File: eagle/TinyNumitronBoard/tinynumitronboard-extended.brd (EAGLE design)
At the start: 100 x 50 mm, 47 parts

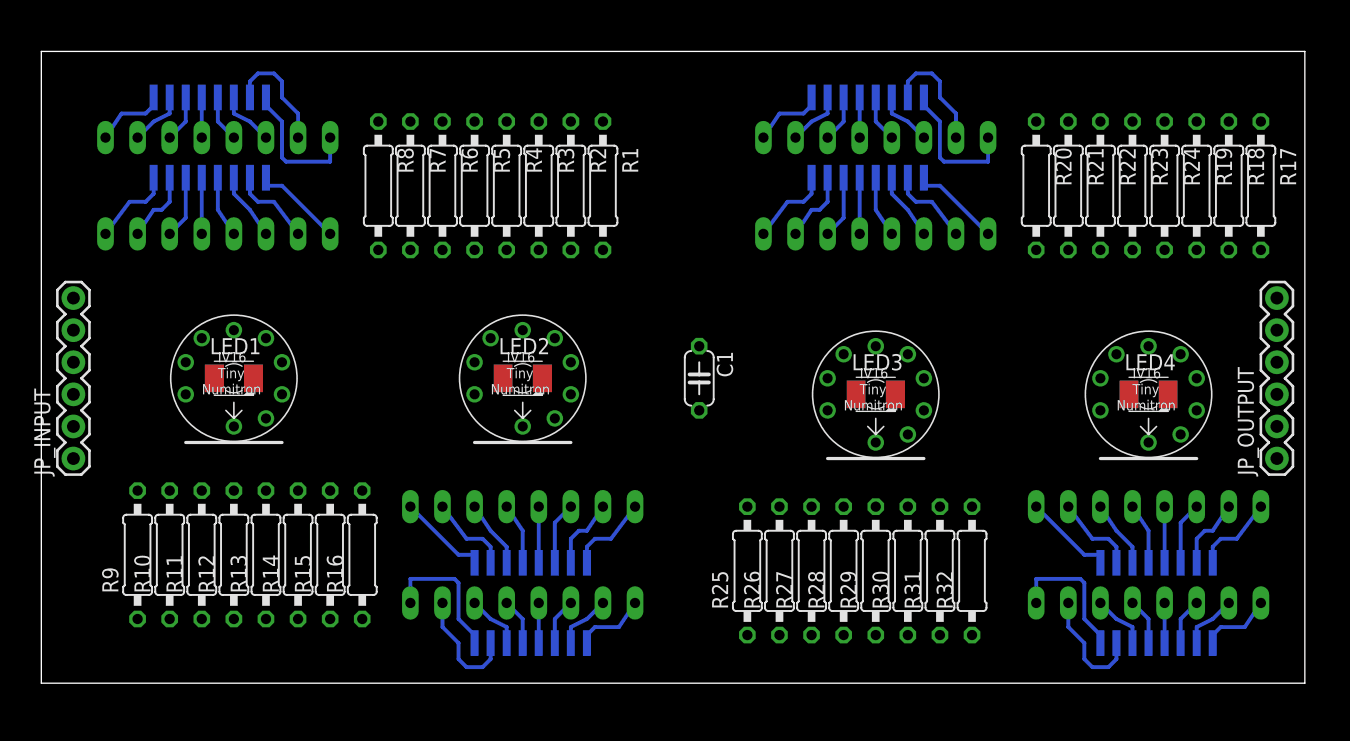
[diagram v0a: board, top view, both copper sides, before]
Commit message: added mounting holes and improved placement.
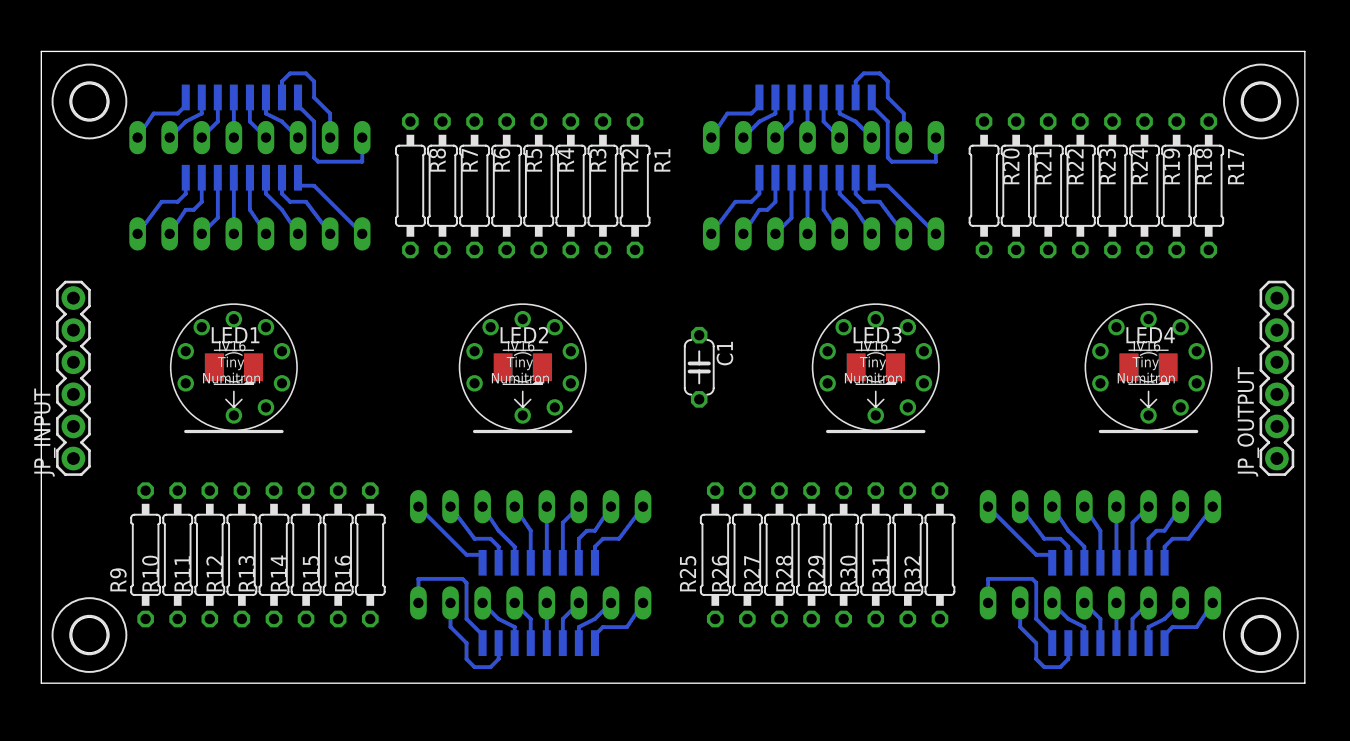
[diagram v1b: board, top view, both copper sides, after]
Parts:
- added H1, H2, H3, H4: MOUNT-HOLE2.8, holes:2,8
- moved R24 4.13 mm to (84.8, 39.4)
- moved U$6 4.13 mm to (61.9, 40.6)
- moved R17 4.13 mm to (92.4, 39.4)
- moved R18 4.13 mm to (89.9, 39.4)
- moved R19 4.13 mm to (87.3, 39.4)
- moved R20 4.13 mm to (74.6, 39.4)
- moved R21 4.13 mm to (77.2, 39.4)
- moved R22 4.13 mm to (79.7, 39.4)
- moved R23 4.13 mm to (82.2, 39.4)
- moved U$8 3.81 mm to (83.8, 8.89)
- moved R29 2.84 mm to (63.5, 10.2)
- moved R31 2.84 mm to (68.6, 10.2)
- moved R25 2.84 mm to (53.3, 10.2)
- moved R26 2.84 mm to (55.9, 10.2)
- moved R27 2.84 mm to (58.4, 10.2)
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
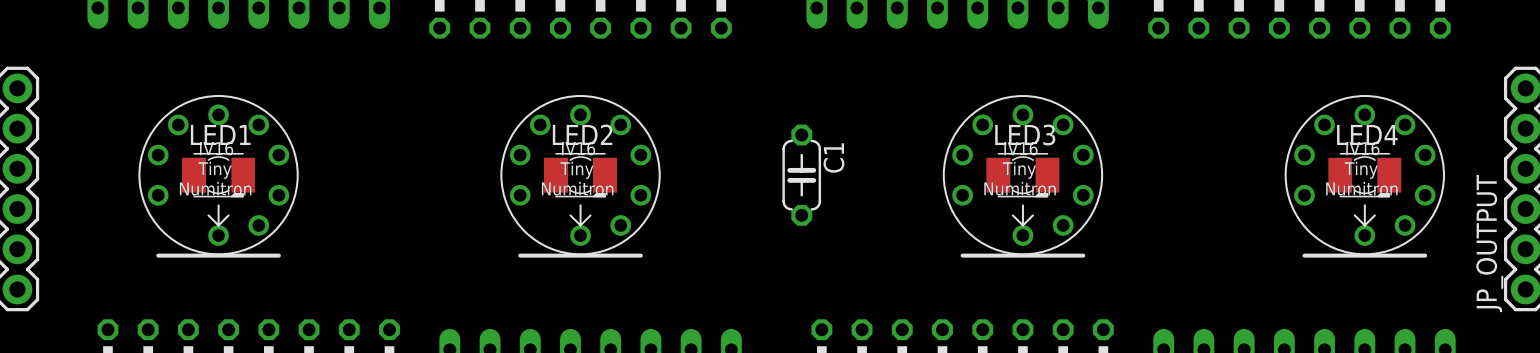
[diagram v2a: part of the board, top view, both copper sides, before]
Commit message: fixed the lots of missing wires ! all connections should be ok now.
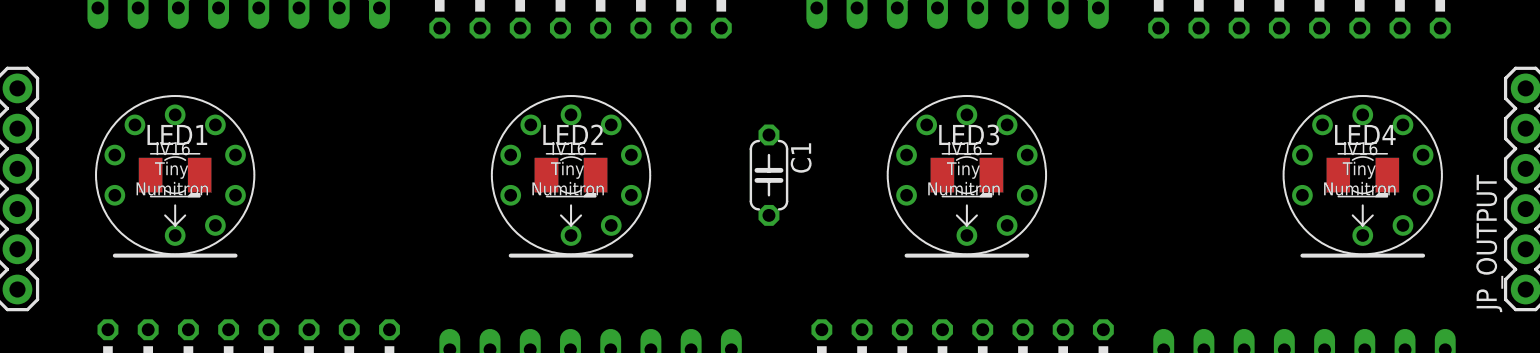
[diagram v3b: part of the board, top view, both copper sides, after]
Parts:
- moved U$2 49.4 mm to (87.5, 25.0)
- moved U$5 28.5 mm to (37.5, 25.0)
- moved U$7 25.1 mm to (62.5, 25.0)
- moved LED3 3.54 mm to (62.5, 25.0)
- moved LED1 2.74 mm to (12.5, 25.0)
- moved U$1 2.74 mm to (12.5, 25.0)
- moved C1 2.07 mm to (50.0, 25.0)
- moved LED2 0.60 mm to (37.5, 25.0)
- moved LED4 0.13 mm to (87.5, 25.0)
- renumbered U$3 to UC1, U$4 to UC4, U$6 to UC2, U$8 to UC3
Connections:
- removed net N$15: JP_INPUT.5, JP_INPUT.6
- removed net N$18: C1.1, JP_INPUT.4, JP_OUTPUT.4, UC4.12, UC4.S12
- removed net N$19: JP_INPUT.3, JP_OUTPUT.3, UC4.11, UC4.S11
- new net N$23: UC1.9, UC1.S9, UC2.14, UC2.S14
- new net N$58: UC2.9, UC2.S9, UC3.14, UC3.S14
- new net RCK: C1.1, JP_INPUT.4, JP_OUTPUT.4, UC1.12, UC1.S12, UC2.12, UC2.S12, UC3.12, UC3.S12, UC4.12, UC4.S12
- new net SCK: JP_INPUT.3, JP_OUTPUT.3, UC1.11, UC1.S11, UC2.11, UC2.S11, UC3.11, UC3.S11, UC4.11, UC4.S11
- new net SER: JP_INPUT.5, JP_INPUT.6, UC1.14, UC1.S14
- net GND: now also UC1.13, UC1.S13, UC2.13, UC2.S13, UC3.13, UC3.S13
- net N$37: now also LED4.A; no longer LED2.A
- net N$54: now also LED2.A; no longer LED3.A
- net N$77: now also LED3.A; no longer LED4.A
- net N$78: now also UC3.9, UC3.S9
- net VCC: now also UC1.10, UC1.S10, UC2.10, UC2.S10, UC3.10, UC3.S10

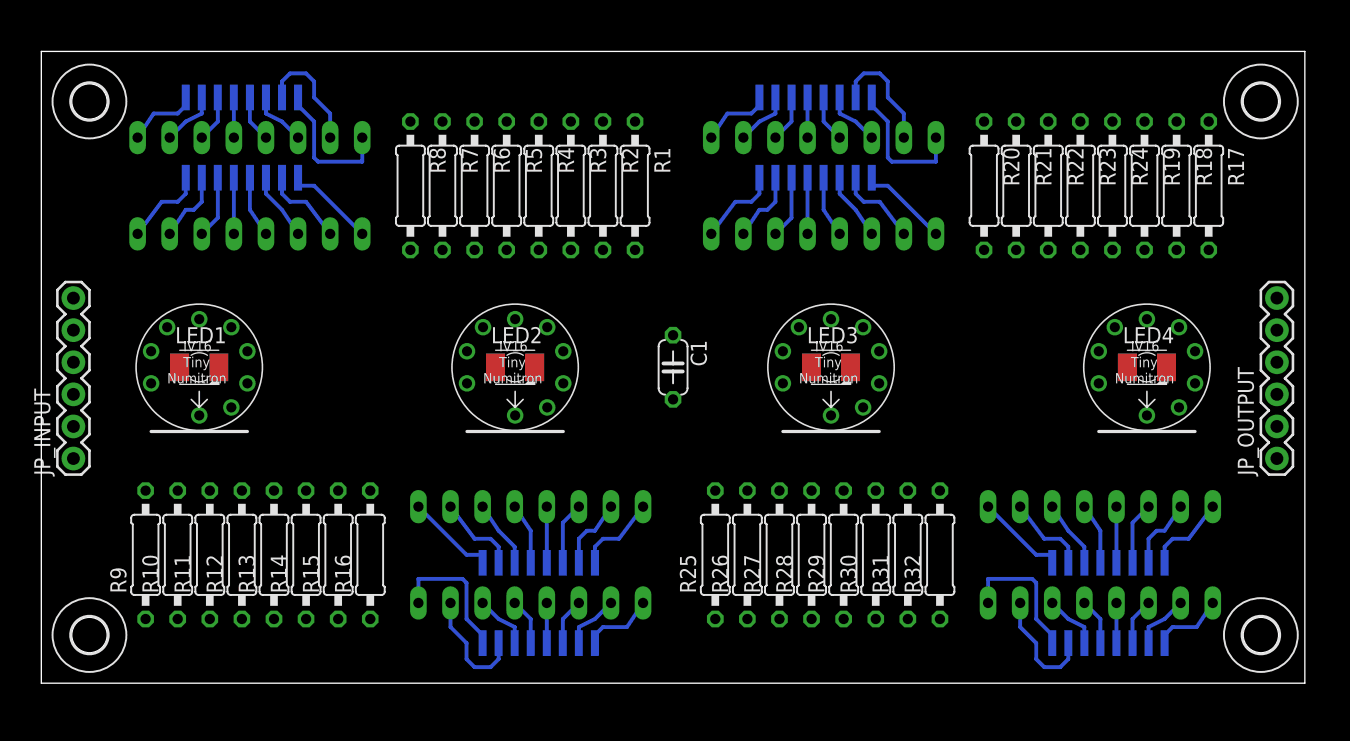
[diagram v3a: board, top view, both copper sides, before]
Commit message: Improved component placement.
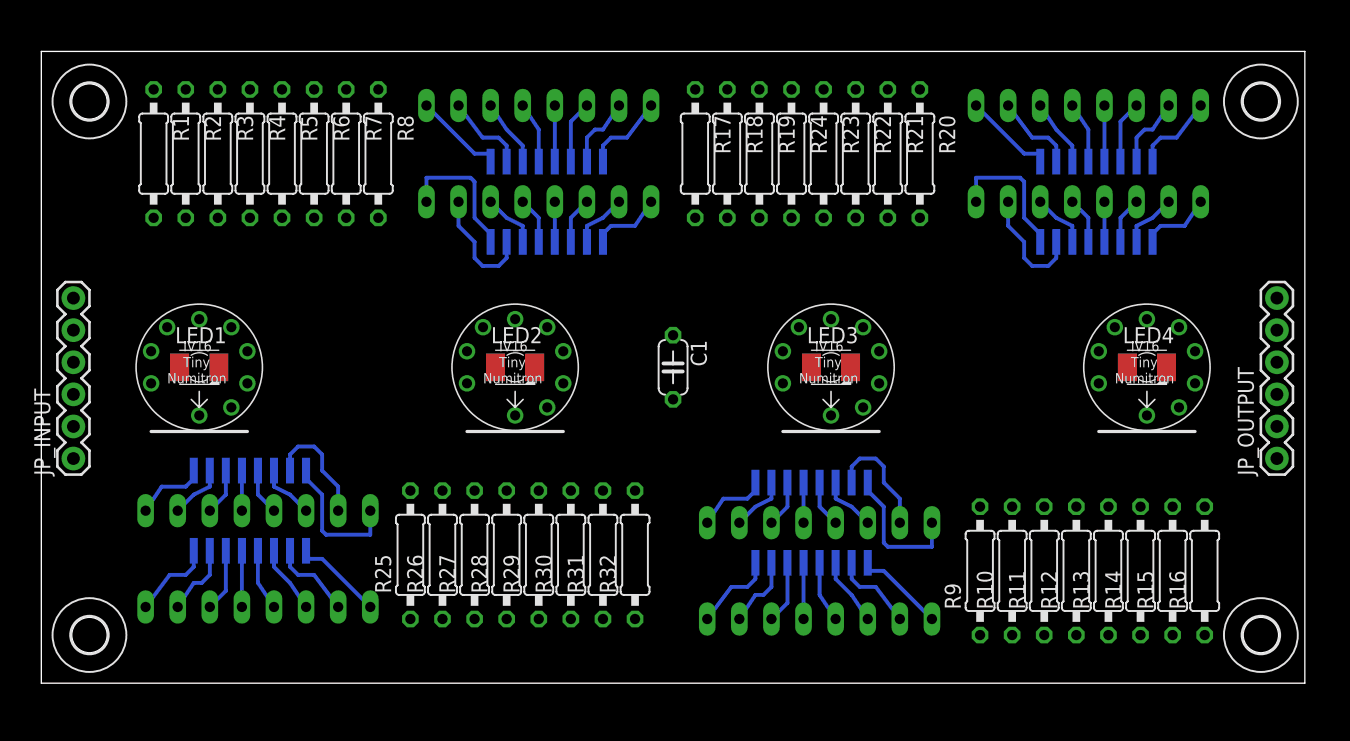
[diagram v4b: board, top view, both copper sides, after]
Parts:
- moved UC3 66.7 mm to (17.1, 11.1), turned to 180 degrees
- moved R12 66.1 mm to (81.9, 8.89)
- moved R14 66.1 mm to (87.0, 8.89)
- moved R16 66.1 mm to (92.1, 8.89)
- moved R9 66.1 mm to (74.3, 8.89)
- moved R10 66.1 mm to (76.8, 8.89)
- moved R11 66.1 mm to (79.4, 8.89)
- moved R13 66.1 mm to (84.5, 8.89)
- moved R15 66.1 mm to (89.5, 8.89)
- moved R17 40.7 mm to (51.8, 41.9)
- moved R1 38.2 mm to (8.89, 41.9)
- moved R18 35.7 mm to (54.3, 41.9)
- moved R2 33.1 mm to (11.4, 41.9)
- moved R19 30.6 mm to (56.8, 41.9)
- moved R3 28.1 mm to (14.0, 41.9)
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
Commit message: did put all the components except the tubes on the bottom.
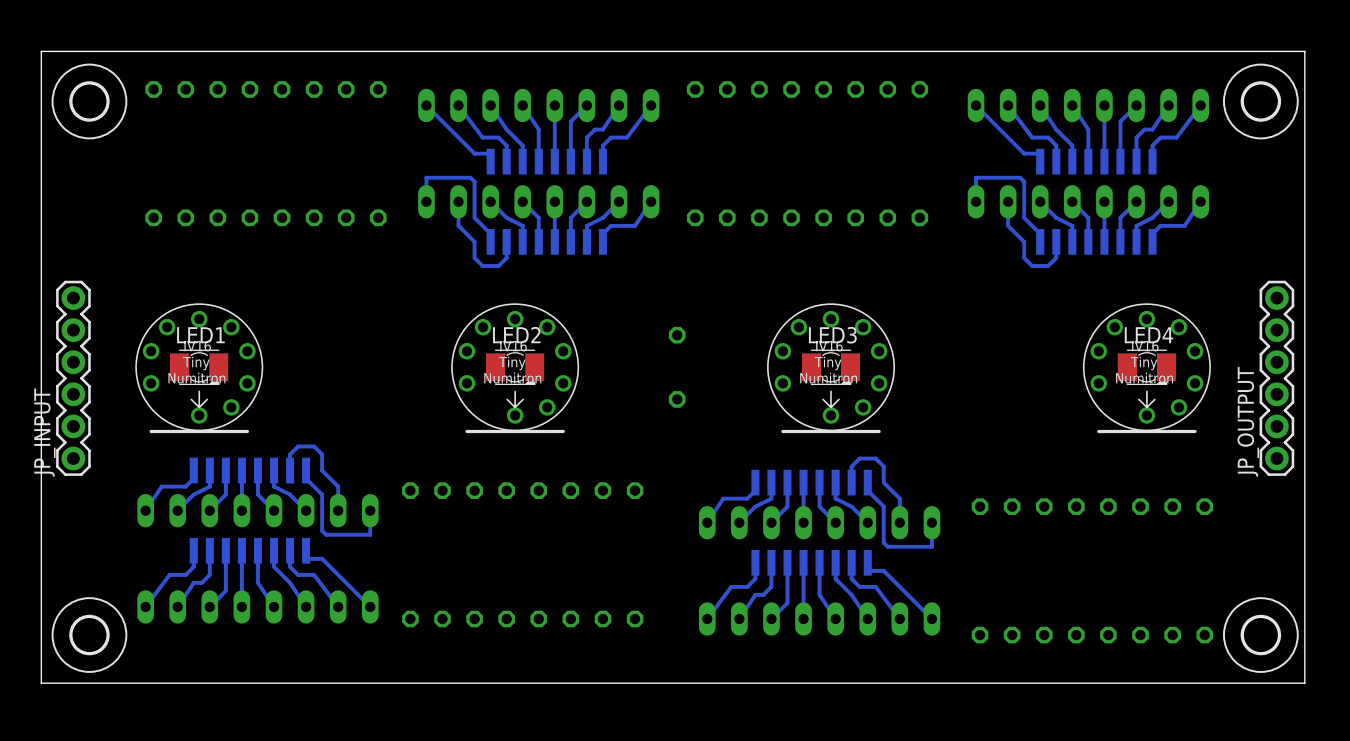
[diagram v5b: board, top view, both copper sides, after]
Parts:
- moved C1 0.33 mm to (50.3, 25.0), flipped to the bottom
- flipped R1 to the bottom
- flipped R10 to the bottom
- flipped R11 to the bottom
- flipped R12 to the bottom
- flipped R13 to the bottom
- flipped R14 to the bottom
- flipped R15 to the bottom
- flipped R16 to the bottom
- flipped R17 to the bottom
- flipped R18 to the bottom
- flipped R19 to the bottom
- flipped R2 to the bottom
- flipped R20 to the bottom
- flipped R21 to the bottom
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
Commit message: Version 1.0 sent to production with nice image on the top.
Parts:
- added U$3: (no value), kalshagar-images:GEARS_1000X500
- R1, R10, R11, R12, R13, R14, R15, R16, R17, R18, R19, R2, R20, R21, R22, R23, R24, R25, R26, R27, R28, R29, R3, R30, R31, R32, R4, R5, R6, R7, R8, R9: value (none) -> RESISTOR_COMBO1206; device resistor:0207/10 -> kalshagar:207-10_SMD_COMBO
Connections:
- net N$1: now also R1.3
- net N$10: now also R3.4
- net N$11: now also R4.4
- net N$12: now also R5.4
- net N$13: now also R6.4
- net N$14: now also R7.4
- net N$16: now also R8.4
- net N$17: now also R8.3
- net N$2: now also R2.3
- net N$20: now also R9.3
- net N$21: now also R10.3
- net N$24: now also R11.3
- net N$25: now also R12.3
- net N$26: now also R13.3
- net N$27: now also R14.3
- net N$28: now also R15.3
- net N$29: now also R9.4
- net N$3: now also R3.3
- net N$30: now also R10.4
- net N$31: now also R11.4
- net N$32: now also R12.4
- net N$33: now also R13.4
- net N$34: now also R14.4
- net N$35: now also R15.4
- net N$36: now also R16.4
- net N$37: now also R16.3
- net N$39: now also R17.3
- net N$4: now also R4.3
- net N$40: now also R18.3
- net N$41: now also R19.3
- net N$42: now also R20.3
- net N$43: now also R21.3
- net N$44: now also R22.3
- net N$45: now also R23.3
- net N$46: now also R17.4
- net N$47: now also R18.4
- net N$48: now also R19.4
- net N$49: now also R20.4
- net N$5: now also R5.3
- net N$50: now also R21.4
- net N$51: now also R22.4
- net N$52: now also R23.4
- net N$53: now also R24.4
- net N$54: now also R24.3
- net N$6: now also R6.3
- net N$62: now also R25.3
- net N$63: now also R26.3
- net N$64: now also R27.3
- net N$65: now also R28.3
- net N$66: now also R29.3
- net N$67: now also R30.3
- net N$68: now also R31.3
- net N$69: now also R25.4
- net N$7: now also R7.3
- net N$70: now also R26.4
- net N$71: now also R27.4
- net N$72: now also R28.4
- net N$73: now also R29.4
- net N$74: now also R30.4
- net N$75: now also R31.4
- net N$76: now also R32.4
- net N$77: now also R32.3
- net N$8: now also R1.4
- net N$9: now also R2.4
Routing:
- net GND: track 0.00 -> 380.4 mm, vias 0 -> 53
- net VCC: track 0.00 -> 338.2 mm, vias 0 -> 8
- net RCK: track 0.00 -> 242.3 mm, vias 0 -> 6
- net SCK: track 0.00 -> 220.2 mm, vias 0 -> 3
- net N$58: track 0.00 -> 107.4 mm, vias 0 -> 5
- net N$68: track 0.00 -> 81.6 mm, vias 0 -> 4
- net N$23: track 0.00 -> 78.4 mm, vias 0 -> 5
- net N$74: track 0.00 -> 68.4 mm, vias 0 -> 1
- net N$22: track 0.00 -> 53.9 mm
- net N$34: track 0.00 -> 52.6 mm, vias 0 -> 1
- net SER: track 0.00 -> 50.3 mm, vias 0 -> 1
- net N$72: track 0.00 -> 49.4 mm, vias 0 -> 3
- net N$36: track 0.00 -> 48.2 mm, vias 0 -> 2
- net N$48: track 0.00 -> 46.0 mm, vias 0 -> 3
- net N$75: track 0.00 -> 44.8 mm, vias 0 -> 2
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- added copper zone on layer 1, net GND
- added copper zone on layer 16, net GND
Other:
- board text added: "1uF"
- board text added: "74xx595"
- board text added: "Alan numitron clock (v1.0 - July 2013)"
- board text added: "All resistors:100Ω LED:470Ω"
- board text added: "CLK"
- board text added: "DATA(in)"
- board text added: "DATA(out)"
- board text added: "Dot/LED"
- board text added: "GND"
- board text added: "LTCH"
- board text added: "VCC"
- board text added: "[IN]"
- board text added: "[OUT]"
- board text added: "http://kalshagar.wikispaces.com/Alan+numitron+clock"
